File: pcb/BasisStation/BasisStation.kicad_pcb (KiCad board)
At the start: 2 copper layers, 160 x 132.6 mm, 80 parts, among them J1 12401598E4-2A, J6 61200621621, Q1 BC337, Q2 BC337, Q3 BC337, Q4 BC337, T1 7499011121A, U1 D3V3XA4B10LP, U6 ESP32-S3-WROOM-1U-N16R8, U7 W5500, Y1 25 MHz

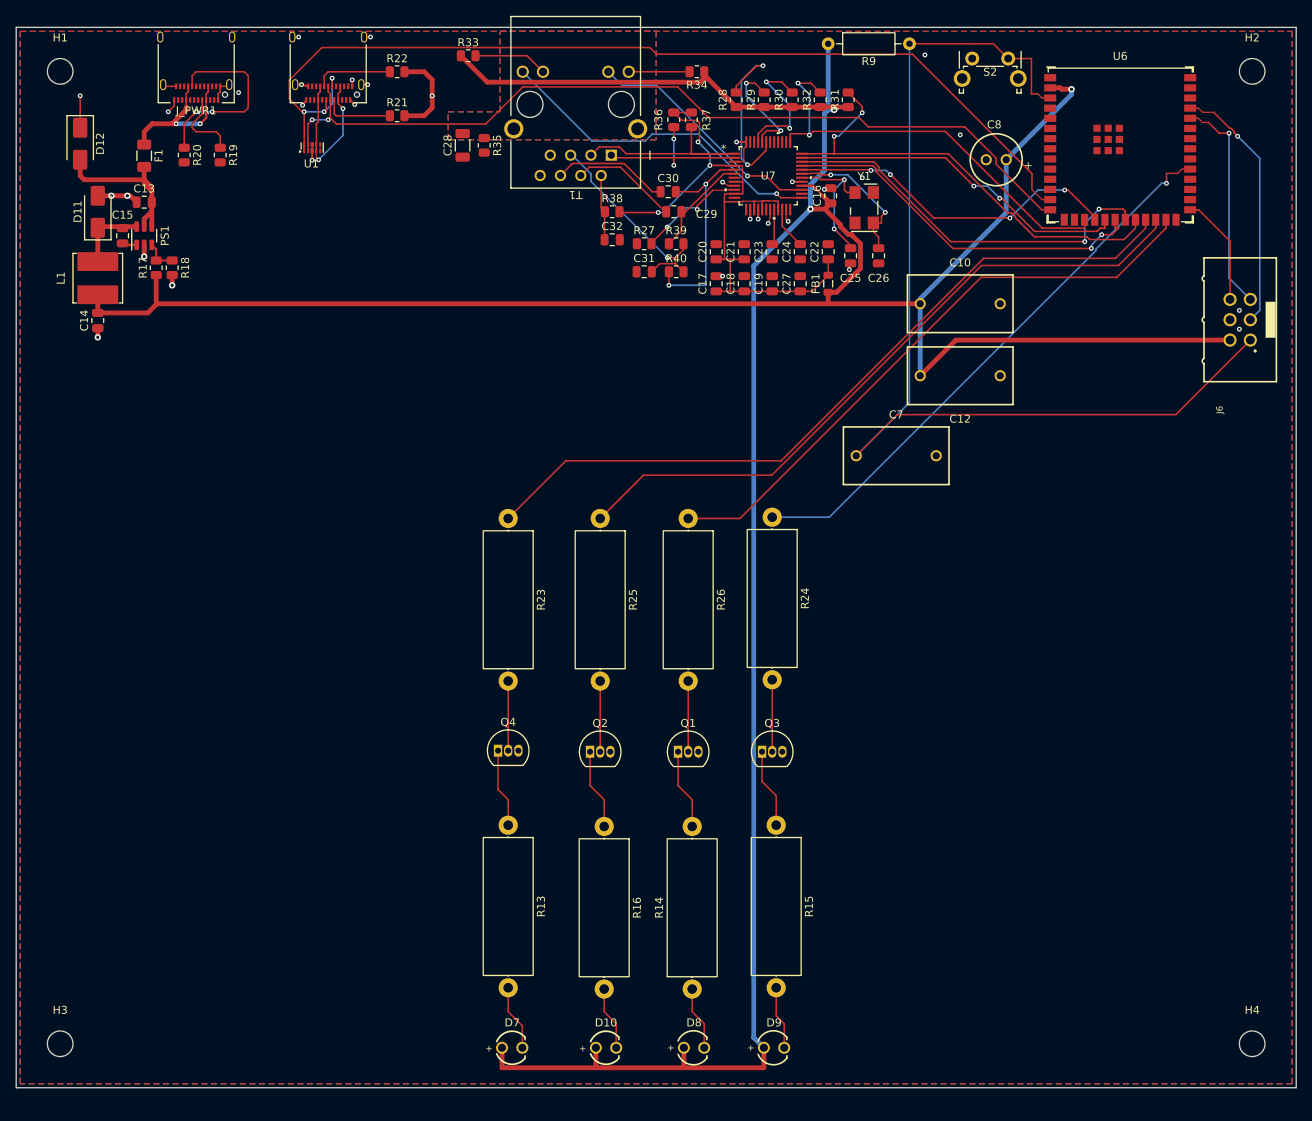
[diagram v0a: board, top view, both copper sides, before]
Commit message: v0.00.001 fix(SHBS-42): Layout an Schaltplan angeglichen und über die Platine verteilt
Buck-Wandler, C7/C10/C12, R9 und J6 in die untere Hälfte verlegt,
Mindestabstand der Courtyards 1 mm. LEDs liegend an der Unterkante,
Linse bündig in der Gehäusewand. Betroffene Netze mit Freerouting
neu geroutet, GND-Insel unter U7 aufgelöst. DRC mit Schaltplan-
abgleich 0/0/0, 17 begründete Ausschlüsse.

Co-Authored-By: Claude Opus 5.5 <noreply@anthropic.com>
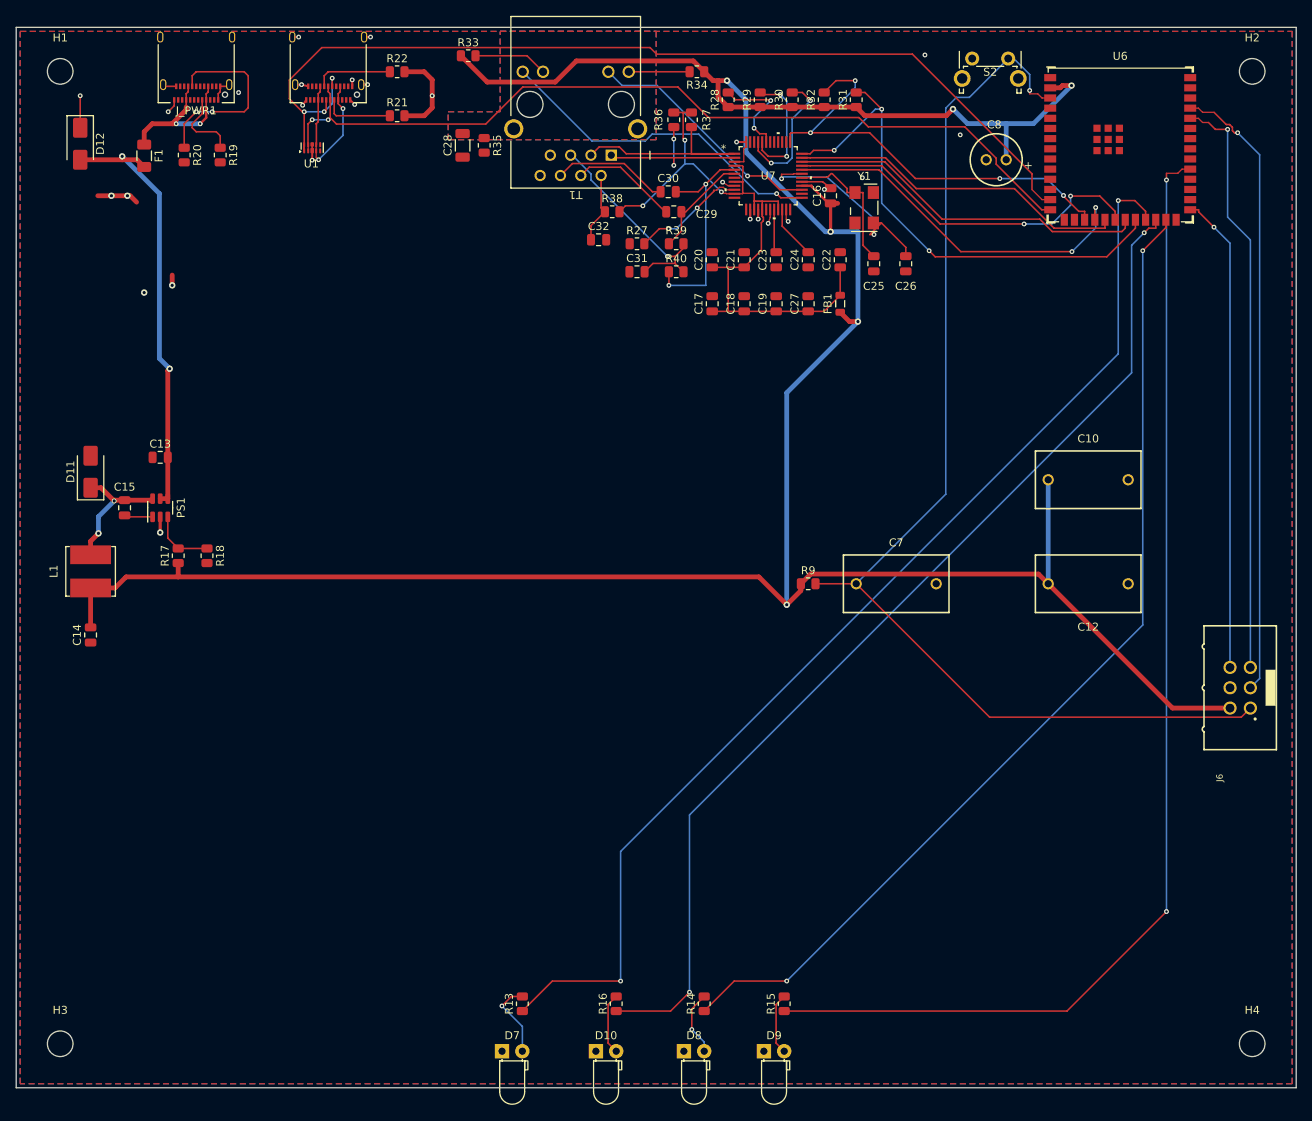
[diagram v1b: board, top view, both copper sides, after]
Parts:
- removed Q1, Q2, Q3, Q4: BC337, Package_TO_SOT_THT:TO-92_Inline
- removed R23, R24, R25, R26: 4,7k, Resistor_THT:R_Axial_DIN0617_L17.0mm_D6.0mm_P20.32mm_Horizontal
- D10, D7: footprint WL-TMRC_3MM:WL-TMRC_3MM -> LED_THT:LED_D3.0mm_Horizontal_O1.27mm_Z2.0mm
- D8, D9: footprint WL-TMRW_3MM:WL-TMRW_3MM -> LED_THT:LED_D3.0mm_Horizontal_O1.27mm_Z2.0mm
- R13, R15, R16: value 220 -> 220Ω; footprint Resistor_THT:R_Axial_DIN0617_L17.0mm_D6.0mm_P20.32mm_Horizontal -> Resistor_SMD:R_0805_2012Metric
- R14: value 220 -> 100Ω; footprint Resistor_THT:R_Axial_DIN0617_L17.0mm_D6.0mm_P20.32mm_Horizontal -> Resistor_SMD:R_0805_2012Metric
- R9: value 10k -> 10kΩ; footprint Resistor_THT:R_Axial_DIN0207_L6.3mm_D2.5mm_P10.16mm_Horizontal -> Resistor_SMD:R_0805_2012Metric
- moved R9 67.5 mm to (149.0, 97.0)
- moved J6 46.0 mm to (203.0, 110.0)
- moved C14 39.3 mm to (59.3, 103.4)
- moved L1 36.7 mm to (59.3, 95.5)
- moved R18 36.3 mm to (73.8, 93.5)
- moved R17 36.1 mm to (70.2, 93.5)
- moved PS1 34.1 mm to (68.0, 87.5)
- moved C15 34.0 mm to (63.5, 87.5)
- moved D11 32.5 mm to (59.3, 83.0)
- moved C13 32.0 mm to (68.0, 81.2)
- moved C12 30.5 mm to (184.0, 97.0)
- moved C10 27.2 mm to (184.0, 84.0)
- moved R13 22.4 mm to (113.3, 149.5), turned to 90 degrees
- moved R15 22.3 mm to (146.0, 149.5), turned to 90 degrees
- moved R16 22.2 mm to (125.0, 149.5), turned to 90 degrees
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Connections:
- D10 pad 1: Net-(D10-K) -> GND
- D10 pad 2: +3V3 -> Net-(D10-A)
- D7 pad 1: Net-(D7-K) -> GND
- D7 pad 2: +3V3 -> Net-(D7-A)
- D8 pad 1: Net-(D8-K) -> GND
- D8 pad 2: +3V3 -> Net-(D8-A)
- D9 pad 1: Net-(D9-K) -> GND
- D9 pad 2: +3V3 -> Net-(D9-A)
- R13 pad 1: Net-(Q4-C) -> Net-(U6-GPIO21)
- R13 pad 2: Net-(D7-K) -> Net-(D7-A)
- R14 pad 1: Net-(D8-K) -> Net-(U6-GPIO48/SPICLK_N/SUBSPICLK_N_DIFF)
- R14 pad 2: Net-(Q1-C) -> Net-(D8-A)
- R15 pad 1: Net-(Q3-C) -> Net-(U6-GPIO38/FSPIWP/SUBSPIWP)
- R15 pad 2: Net-(D9-K) -> Net-(D9-A)
- R16 pad 1: Net-(Q2-C) -> Net-(U6-GPIO47/SPICLK_P/SUBSPICLK_P_DIFF)
- R16 pad 2: Net-(D10-K) -> Net-(D10-A)
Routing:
- net +3V3: track 445.7 -> 357.5 mm, vias 3 -> 6
- net Net-(U6-GPIO38/FSPIWP/SUBSPIWP): track 71.1 -> 148.4 mm, vias 1 -> 2
- net Net-(U6-GPIO48/SPICLK_N/SUBSPICLK_N_DIFF): track 75.8 -> 126.7 mm, vias 0 -> 2
- net Net-(U6-GPIO21): track 95.8 -> 142.2 mm, vias 0 -> 2
- net Net-(J6-Pin_3): track 32.1 -> 78.4 mm
- net Net-(J6-Pin_5): track 27.5 -> 73.7 mm
- net Net-(J6-Pin_6): track 13.9 -> 59.9 mm, vias 0 -> 1
- net Net-(U6-GPIO47/SPICLK_P/SUBSPICLK_P_DIFF): track 85.5 -> 131.3 mm, vias 0 -> 2
- net /Stromversorgung/+5V: track 22.2 -> 55.1 mm, vias 0 -> 2
- net /Layout/EN: track 132.5 -> 144.9 mm, vias 0 -> 1
- net Net-(U7-PMODE2): track 23.6 -> 12.9 mm
- net Net-(Q1-C): track 10.1 -> 0.00 mm
- net Net-(Q2-C): track 10.1 -> 0.00 mm
- net Net-(Q3-C): track 9.91 -> 0.00 mm
- net Net-(Q4-C): track 9.85 -> 0.00 mm
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
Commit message: v0.00.001 fix(SHBS-52): ESP32-S3 in die rechte Platinenhälfte verlegt
U6 bei 185/90, um 90 Grad gedreht, U.FL-Stecker zur rechten Wand.
C8 und C7/R9 über U6 an den Pins, C10/C12 darunter. Netze von U6 neu
geroutet, GND-Insel an U1 aufgelöst, J6-Pad 4 per Via angebunden.
DRC mit Schaltplanabgleich 0/0/0.

Co-Authored-By: Claude Opus 5.5 <noreply@anthropic.com>
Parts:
- moved U6 48.1 mm to (185.0, 90.0), turned to -90 degrees
- moved C8 36.3 mm to (193.0, 74.0)
- moved C7 29.2 mm to (178.0, 74.0)
- moved R9 29.2 mm to (167.0, 74.0), turned to 90 degrees
- moved C10 24.7 mm to (178.0, 108.0)
- moved C12 22.3 mm to (178.0, 118.5)
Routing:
- net Net-(U6-GPIO38/FSPIWP/SUBSPIWP): track 148.4 -> 82.1 mm
- net Net-(J6-Pin_3): track 78.4 -> 20.1 mm, vias 1 -> 0
- net Net-(U6-GPIO21): track 142.2 -> 91.0 mm
- net Net-(U6-GPIO48/SPICLK_N/SUBSPICLK_N_DIFF): track 126.7 -> 75.9 mm
- net Net-(J6-Pin_5): track 73.7 -> 23.1 mm
- net Net-(U6-GPIO47/SPICLK_P/SUBSPICLK_P_DIFF): track 131.3 -> 83.8 mm
- net USB+: track 109.5 -> 138.0 mm, vias 2 -> 3
- net Net-(J6-Pin_6): track 59.9 -> 31.6 mm
- net /Layout/EN: track 144.9 -> 117.0 mm
- net ETH_MOSI: track 42.6 -> 65.5 mm, vias 0 -> 2
- net ETH_INT: track 65.1 -> 86.5 mm
- net ETH_MISO: track 45.3 -> 66.4 mm, vias 0 -> 2
- net ETH_SCLK: track 46.1 -> 63.7 mm
- net ETH_RST: track 56.4 -> 72.4 mm, vias 4 -> 3
- net ETH_SCSn: track 46.3 -> 60.8 mm, vias 2 -> 4
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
